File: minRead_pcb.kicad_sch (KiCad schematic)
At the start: 111 parts, among them J1 USB_C_Receptacle, J2 FH34SRJ-24S-0.5SH_50_, J3 FH34SRJ-6S-0.5SH_50_, J5 Conn_01x02, J7 Micro_SD_Card, Q10 BSS138, Q11 BSS138, Q16 MMBT3906, Q17 MMBT3904, Q18 AO3419, Q4 [BSS138] AO3400A, Q5 AO3419, Q6 AO3419, SW1 SW_Push, SW10 SW_Push, SW11 SW_Push, SW2 SW_Push, SW3 SW_Push, SW4 SW_Push, SW6 SW_Push, SW8 SW_Push, SW9 SW_Push, U1 TPD4E1U06DBVR, U11 AP3031KTR, U3 AP2112K-3.3, U4 ESP32-S3-WROOM-1, U6 TPD4E1U06DBVR, U7 TP4054

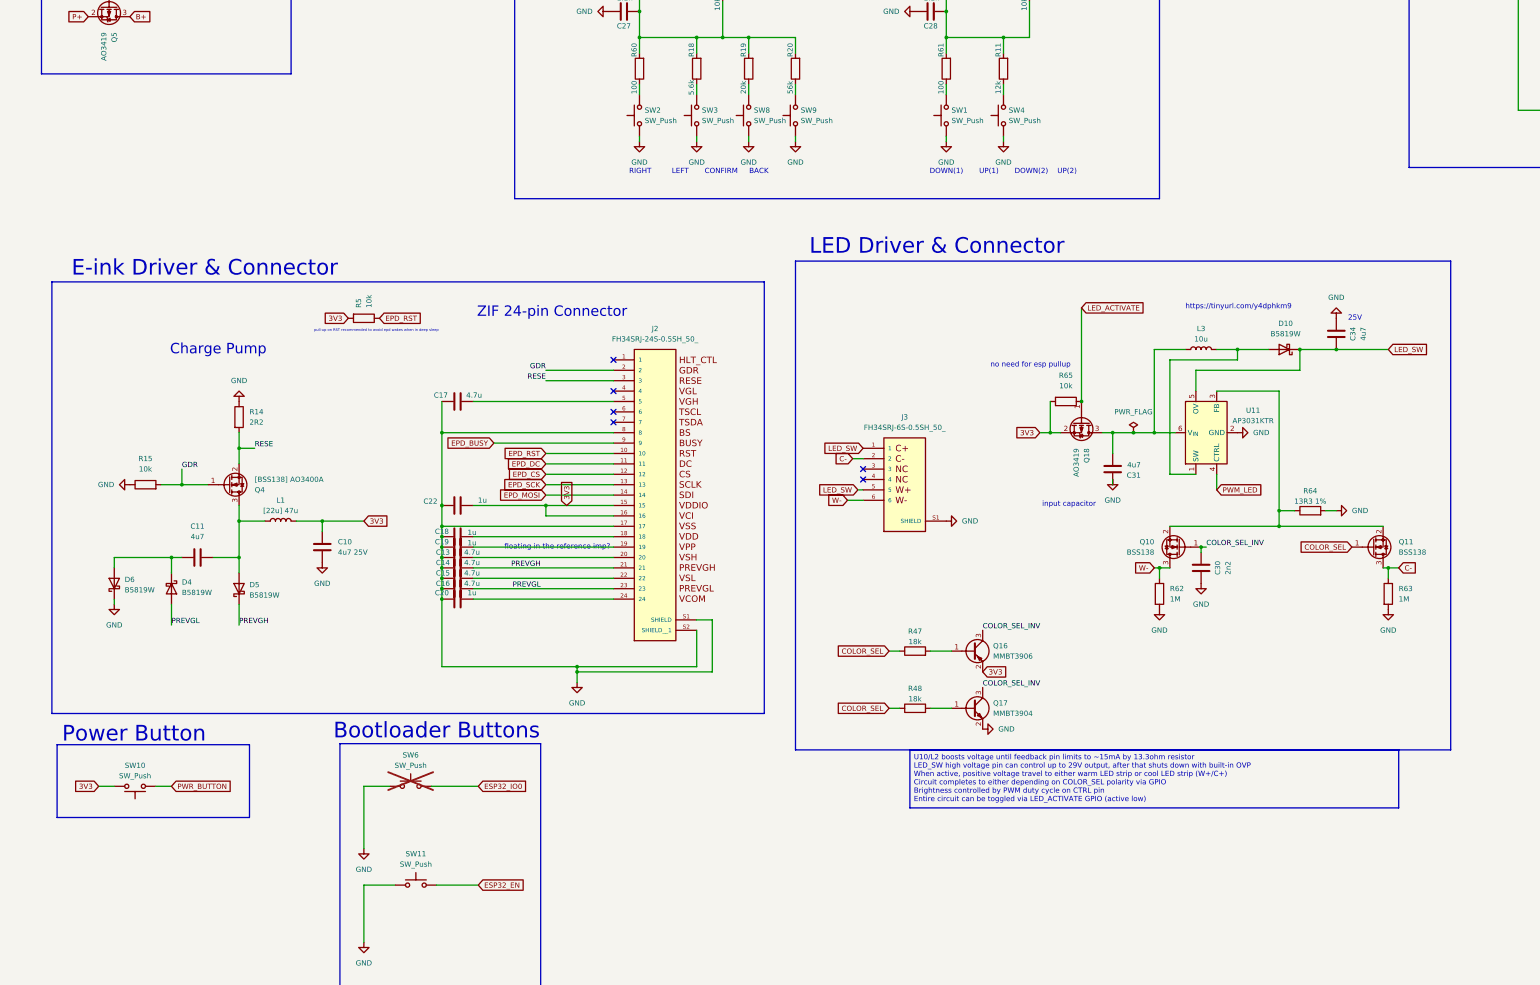
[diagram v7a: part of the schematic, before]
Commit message: mostly fin, some edge cut changes
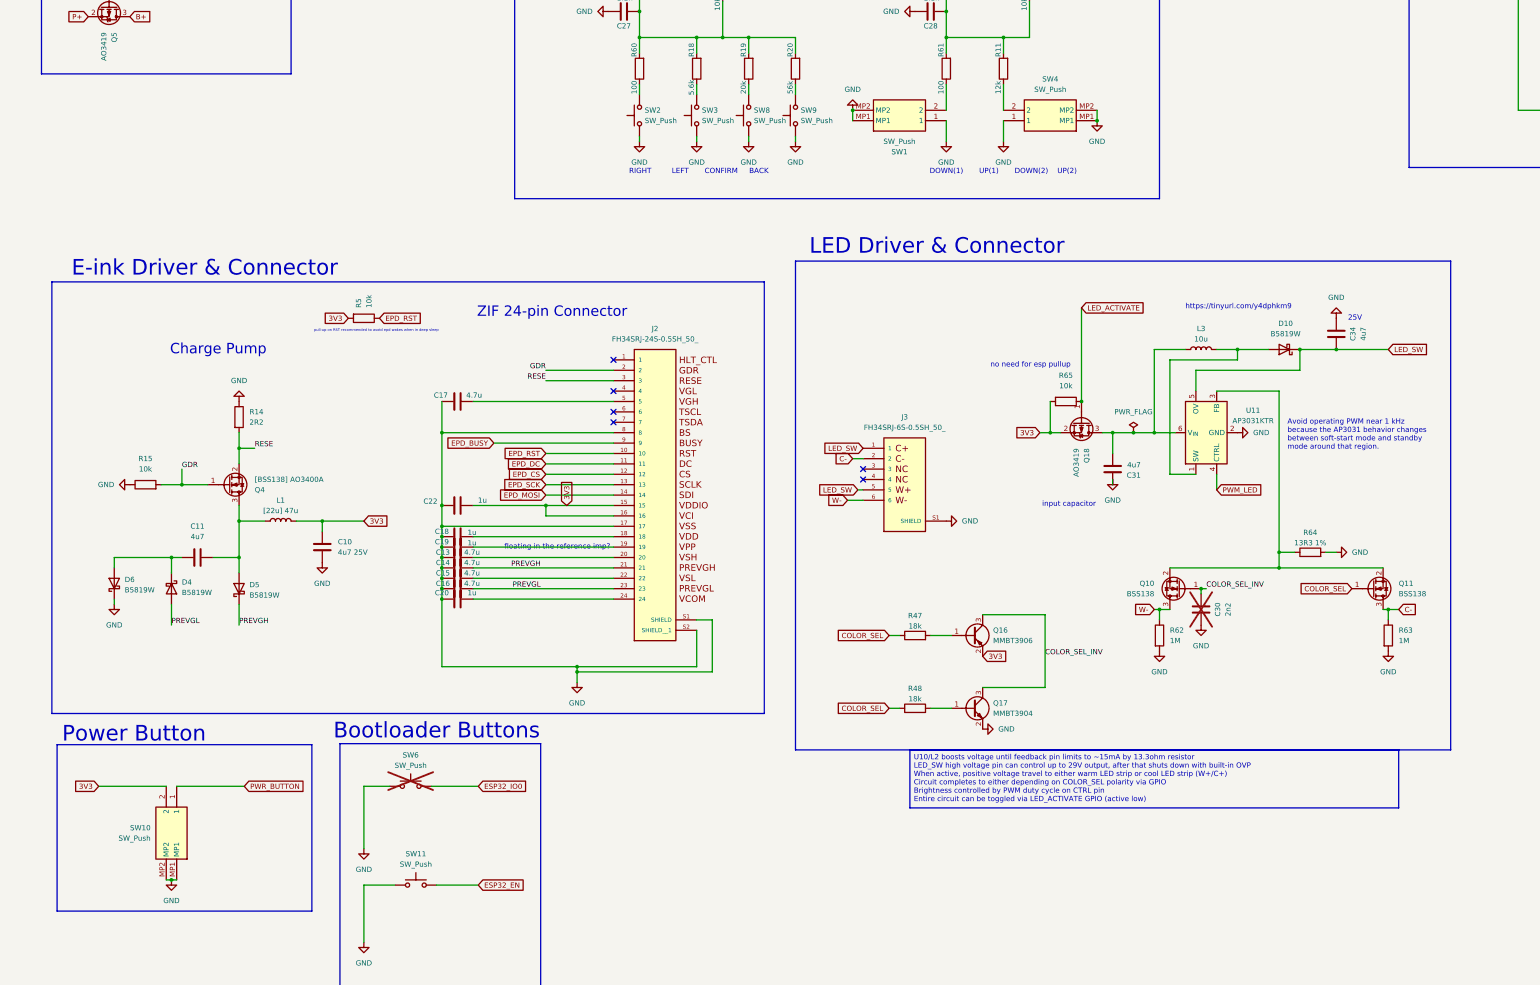
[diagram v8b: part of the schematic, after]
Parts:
- C30: now not fitted
- SW1, SW10, SW4: footprint DEAN:SKSNLAE010 -> SKSNLAE010; symbol Switch:SW_Push -> DEAN:SKSNLAE010; Height (none) -> 3.5; Manufacturer_Name (none) -> ALPS Electric; Manufacturer_Part_Number (none) -> SKSNLAE010; Mouser Part Number (none) -> 688-SKSNLAE010; Mouser Price/Stock (none) -> https://www.mouser.co.uk/ProductDetail/Alps-Alpine/SKSNLAE0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
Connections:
- net GND: now also SW1.MP1, SW1.MP2, SW10.MP1, SW10.MP2, SW4.MP1, SW4.MP2
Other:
- note added: "Avoid operating PWM near 1 kHz because the AP3031 behavior changes between soft-start mode and standby mode around that region."
- moved on the sheet: Q10, Q11, Q16, R47, R62, R63, R64
